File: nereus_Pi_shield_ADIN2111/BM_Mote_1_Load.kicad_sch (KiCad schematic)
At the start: 10 parts, among them U9 FPF2700MX

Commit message: S5.a: payload load switch U9 FPF2700MX (obsolete) -> U11 TPS26621DRCR; R11 DNP; Sofar brief
Load Switch sheet: U11 TI TPS26621DRCR (JLC C1848341) on new project
symbol nereus:TPS26621DRCR, stock Texas_DRC0010J footprint; R34 9.09k
(0.73 A); R41 1M IN->UVLO; dVdT NC; R32 pull-up -> R42 pull-down (SHDN
active low, payload off by default); SW_PGOOD/R33/TP34 removed. Top-Level:
R11 DNP, SW_PGOOD sheet pin removed. D18. ERC 74/626, netcheck 50/50,
kept parts identical. New docs/design-review/sofar_brief.md (mote vs
shield deviations for Sofar) + TRACKER rule.

Co-Authored-By: Claude Opus 5.5 <noreply@anthropic.com>
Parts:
- removed R33: RMCF0402FT100K, FP-RMCF0402-IPC_C, symbol BM_Mote_000639-AB-altium-import:Load_1_1029c3af85768c4190bb7ad29bc67b5_Altium C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
- removed TP34: TEST_POINT, PCB_TP_1.5mm, symbol BM_Mote_000639-AB-altium-import:Load_1_TEST_POINT_Sofar Ocean Technologies, Inc.
- removed U9: FPF2700MX, FAIR-SO-8_V, symbol BM_Mote_000639-AB-altium-import:Load_0_FAIR-FPF27XX-SOP-8_Altium Content Vault
- added R41: 1M, Resistor_SMD:R_0402_1005Metric, symbol Device:R
- added U11: TPS26621DRCR, Package_SON:Texas_DRC0010J, symbol nereus:TPS26621DRCR
- R34: value RC0402FR-07374KL -> RC0402FR-079K09L; RESISTANCE 374k -> 9.09kR
- renumbered R32 to R42
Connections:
- net GND: now also U11.11 (EP), U11.3 (OVP), U11.5 (RTN), U11.6 (GND)
- net ISET: now also U11.7 (ILIM)
- net SW_EN: now also U11.4 (~{SHDN})
- net SW_FLAGB: now also U11.9 (~{FLT})
- net VBUS_OUT: now also U11.10 (OUT)
- net VIN: now also R41.1, U11.1 (IN)
- new net: R41.2, U11.2 (UVLO)
- no-connect marks 0 -> 1

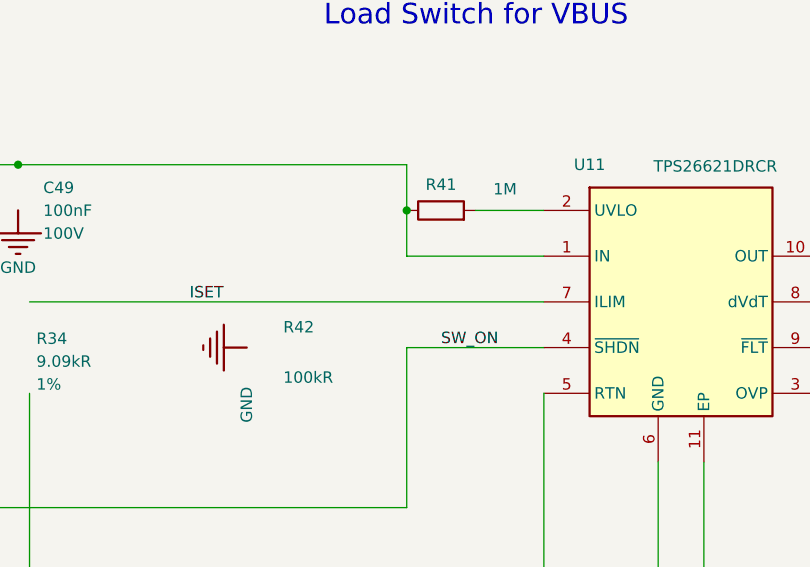
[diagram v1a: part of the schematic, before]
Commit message: S5.a: fix QE round 1 (R34 PART NUMBER, R42 10k worst-case SHDN, RTN=GND, N6, stale docs)
Co-Authored-By: Claude Opus 5.5 <noreply@anthropic.com>
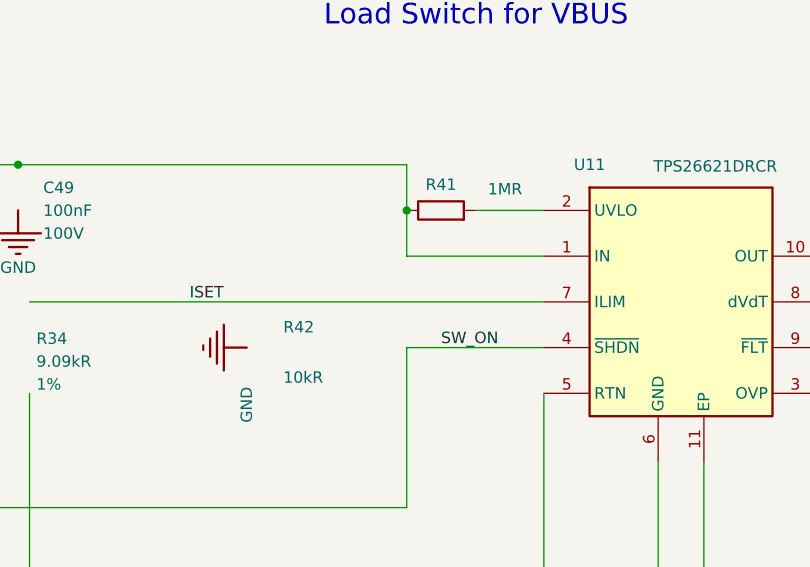
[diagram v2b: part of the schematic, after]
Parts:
- R34: PART NUMBER RC0402FR-07374KL -> RC0402FR-079K09L
- R41: value 1M -> RC0402FR-071ML; MPN RC0402FR-071ML -> (none); PART NUMBER (none) -> RC0402FR-071ML; RESISTANCE (none) -> 1MR
- R42: value RMCF0402FT100K -> RMCF0402FT10K0; RESISTANCE 100kR -> 10kR
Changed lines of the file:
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@@
 			)
 		)
-		(property "Value" "RMCF0402FT100K"
+		(property "Value" "RMCF0402FT10K0"
 			(at 177.292 153.2382 0)
 			(effects
@@
 			)
 		)
-		(property "Description" "RES 100K OHM 1% 0402: SW_ON pull-down, payload off by default (TPS26621 SHDN active low, D18)"
+		(property "Description" "RES 10K OHM 1% 0402: SW_ON pull-down, payload off by default. Worst case SHDN source 10 uA x 10k = 0.1 V < V(SHUTF) min 0.9 V (SLVSDT4F 7.5, D18)"
 			(at 195.58 154.7622 0)
 			(effects
@@
 			)
 		)
-		(property "RESISTANCE" "100kR"
+		(property "RESISTANCE" "10kR"
 			(at 181.864 158.8262 0)
 			(effects
@@
 			)
 		)
-		(property "PART NUMBER" "RC0402FR-07374KL"
+		(property "PART NUMBER" "RC0402FR-079K09L"
 			(at 152.908 149.1742 0)
 			(effects
@@
 			)
 		)
-		(property "Value" "1M"
+		(property "Value" "RC0402FR-071ML"
 			(at 206.502 137.16 90)
 			(effects
@@
 					(size 1.27 1.27)
 				)
+				(hide yes)
 			)
 		)
@@
 			)
 		)
-		(property "MPN" "RC0402FR-071ML"
-			(at 199.39 139.5222 0)
-			(effects
-				(font
-					(size 1.27 1.27)
-				)
-				(hide yes)
-			)
-		)
 		(property "MANUFACTURER" "Yageo"
 			(at 199.39 139.5222 0)
 			(effects
+				(font
+					(size 1.27 1.27)
+				)
+				(hide yes)
+			)
+		)
+		(property "RESISTANCE" "1MR"
+			(at 206.502 137.16 90)
+			(effects
+				(font
+					(size 1.27 1.27)
+				)
+			)
+		)
+		(property "PART NUMBER" "RC0402FR-071ML"
+			(at 199.39 139.5222 0)
+			(effects

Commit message: S4.d: footprints findable -- project library Vault (mote.pretty) extracted from the mote board; close S5.a
43 footprints the schematic uses, extracted read-only from the reference
board with KiCad 9.0.6 pcbnew (tools/fpextract.py, back-side parts
flipped, nets cleared), registered as nickname Vault to match the board
IDs; 118 bare footprint fields -> Vault:<name>. fpextract --verify: 0
problems (negative-tested). Netlist identical except footprint fields.
ERC 74/626 -> 74/508 (footprint-link warnings gone). D19.

Co-Authored-By: Claude Opus 5.5 <noreply@anthropic.com>
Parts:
- C49, C50: footprint FP-GRM188-0_1-e0_2_0_5-IPC_B -> Vault:FP-GRM188-0_1-e0_2_0_5-IPC_B
- D3: footprint FP-PMDTM-MFG -> Vault:FP-PMDTM-MFG
- R34: footprint RESC1005X40X25LL05T10 -> Vault:RESC1005X40X25LL05T10
- R35, R42: footprint FP-RMCF0402-IPC_C -> Vault:FP-RMCF0402-IPC_C
- TP35: footprint PCB_TP_1.5mm -> Vault:PCB_TP_1.5mm
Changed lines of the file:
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@@
 			)
 		)
-		(property "Footprint" ""
+				(property "Footprint" ""
 			(at 292.1 149.6822 0)
 			(effects
@@
 			)
 		)
-		(property "Footprint" "PCB_TP_1.5mm"
+		(property "Footprint" "Vault:PCB_TP_1.5mm"
 			(at 279.4 175.0822 0)
 			(effects
@@
 			)
 		)
-		(property "Footprint" ""
+				(property "Footprint" ""
 			(at 196.85 180.1622 0)
 			(effects
@@
 			)
 		)
-		(property "Footprint" "FP-RMCF0402-IPC_C"
+		(property "Footprint" "Vault:FP-RMCF0402-IPC_C"
 			(at 195.58 154.7622 0)
 			(effects
@@
 			)
 		)
-		(property "Footprint" "FP-RMCF0402-IPC_C"
+		(property "Footprint" "Vault:FP-RMCF0402-IPC_C"
 			(at 279.4 172.5422 0)
 			(effects
@@
 			)
 		)
-		(property "Footprint" ""
+				(property "Footprint" ""
 			(at 177.8 154.7622 0)
 			(effects
@@
 			)
 		)
-		(property "Footprint" ""
+				(property "Footprint" ""
 			(at 152.4 139.5222 0)
 			(effects
@@
 			)
 		)
-		(property "Footprint" "FP-PMDTM-MFG"
+		(property "Footprint" "Vault:FP-PMDTM-MFG"
 			(at 292.1 149.6822 0)
 			(effects
@@
 			)
 		)
-		(property "Footprint" ""
+				(property "Footprint" ""
 			(at 271.78 139.5222 0)
 			(effects
@@
 			)
 		)
-		(property "Footprint" "FP-GRM188-0_1-e0_2_0_5-IPC_B"
+		(property "Footprint" "Vault:FP-GRM188-0_1-e0_2_0_5-IPC_B"
 			(at 271.78 134.4422 0)
 			(effects
@@
 			)
 		)
-		(property "Footprint" "RESC1005X40X25LL05T10"
+		(property "Footprint" "Vault:RESC1005X40X25LL05T10"
 			(at 151.13 157.3022 0)
 			(effects
@@
 			)
 		)
-		(property "Footprint" ""
+				(property "Footprint" ""
 			(at 279.4 154.7622 0)
 			(effects
@@
 			)
 		)
-		(property "Footprint" "FP-GRM188-0_1-e0_2_0_5-IPC_B"
+		(property "Footprint" "Vault:FP-GRM188-0_1-e0_2_0_5-IPC_B"
 			(at 152.4 134.4422 0)
 			(effects
@@
 			)
 		)
-		(property "Footprint" "Package_SON:Texas_DRC0010J"
+				(property "Footprint" "Package_SON:Texas_DRC0010J"
 			(at 226.06 149.6822 0)
 			(effects
@@
 			)
 		)
-		(property "Footprint" "Resistor_SMD:R_0402_1005Metric"
+				(property "Footprint" "Resistor_SMD:R_0402_1005Metric"
 			(at 199.39 139.5222 0)
 			(effects

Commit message: S5.h: BOM alternates as hidden ALT/SOURCING fields; tracked bom.csv
- 24 flagged passives: hidden ALT1/ALT2 MPN/MFR/LCSC, ALT NOTE, SOURCING
  (values from docs/design-review/bom_alternates.md, D26)
- Critical parts (U1-U3, L3/L6, Y1, D1-D3, MP1-MP4, J5, J1): SOURCING only
- tools/check.sh exports docs/design-review/bom.csv: specified part first,
  alternates beside it; grouped by Value + DNP (R11 apart from R12/R13/R17/R19)
- J1 Footprint property re-indented (whitespace; import leftover)
- Fields only: ERC 531/27/504 unchanged, netcheck 51/51, midwire 0;
  netlist diff = the 208 new fields
- Docs: bom_alternates, bom_lifecycle, sofar_brief, changelog, DESIGN,
  TRACKER, viewer, DEV_LOG

Co-Authored-By: Claude Opus 5.5 <noreply@anthropic.com>
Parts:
- D3: SOURCING (none) -> JLC global sourcing (D26); no LCSC listing
- R34: ALT NOTE (none) -> 9.09 kΩ ±1 % 62.5 mW 50 V ±100 ppm thick film; our part (D1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; ALT1 LCSC (none) -> C227284; ALT1 MFR (none) -> YAGEO; ALT1 MPN (none) -> AC0402FR-079K09L; ALT2 LCSC (none) -> C11549; ALT2 MFR (none) -> UNI-ROYAL; ALT2 MPN (none) -> 0402WGF9091TCE; SOURCING (none) -> JLC global sourcing (first build) until an ALT is approved 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
- R35: ALT NOTE (none) -> 100 kΩ ±1 % 62.5 mW 50 V ±100 ppm; ALT1 is JLC Basic; AEC-Q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; ALT1 LCSC (none) -> C25741; ALT1 MFR (none) -> UNI-ROYAL; ALT1 MPN (none) -> 0402WGF1003TCE; ALT2 LCSC (none) -> C60491; ALT2 MFR (none) -> YAGEO; ALT2 MPN (none) -> RC0402FR-07100KL; SOURCING (none) -> JLC global sourcing (first build) until an ALT is approved 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
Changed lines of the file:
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@@
+			)
+		)
+		(property "ALT1 MPN" "0402WGF1003TCE"
+			(at 279.4 172.5422 0)
+			(effects
+				(font
+					(size 1.27 1.27)
+				)
+				(hide yes)
+			)
+		)
+		(property "ALT1 MFR" "UNI-ROYAL"
+			(at 279.4 172.5422 0)
+			(effects
+				(font
+					(size 1.27 1.27)
+				)
+				(hide yes)
+			)
+		)
+		(property "ALT1 LCSC" "C25741"
+			(at 279.4 172.5422 0)
+			(effects
+				(font
+					(size 1.27 1.27)
+				)
+				(hide yes)
+			)
+		)
+		(property "ALT2 MPN" "RC0402FR-07100KL"
+			(at 279.4 172.5422 0)
+			(effects
+				(font
+					(size 1.27 1.27)
+				)
+				(hide yes)
+			)
+		)
+		(property "ALT2 MFR" "YAGEO"
+			(at 279.4 172.5422 0)
+			(effects
+				(font
+					(size 1.27 1.27)
+				)
+				(hide yes)
+			)
+		)
+		(property "ALT2 LCSC" "C60491"
+			(at 279.4 172.5422 0)
+			(effects
+				(font
+					(size 1.27 1.27)
+				)
+				(hide yes)
+			)
+		)
+		(property "ALT NOTE" "100 kΩ ±1 % 62.5 mW 50 V ±100 ppm; ALT1 is JLC Basic; AEC-Q200 not stated (Stackpole is)"
+			(at 279.4 172.5422 0)
+			(effects
+				(font
+					(size 1.27 1.27)
+				)
+				(hide yes)
+			)
+		)
+		(property "SOURCING" "JLC global sourcing (first build) until an ALT is approved (D26)"
+			(at 279.4 172.5422 0)
+			(effects
+				(font
+					(size 1.27 1.27)
+				)
+				(hide yes)
 			)
 		)
@@
 			)
 		)
+		(property "SOURCING" "JLC global sourcing (D26); no LCSC listing"
+			(at 292.1 149.6822 0)
+			(effects
+				(font
+					(size 1.27 1.27)
+				)
+				(hide yes)
+			)
+		)
 		(pin "2"
 		)
@@
 				(hide yes)
 			)
+		)
+		(property "ALT1 MPN" "AC0402FR-079K09L"
+			(at 151.13 157.3022 0)
+			(effects
+				(font
+					(size 1.27 1.27)
+				)
+				(hide yes)
+			)
+		)
+		(property "ALT1 MFR" "YAGEO"
+			(at 151.13 157.3022 0)
+			(effects
+				(font
+					(size 1.27 1.27)
+				)
+				(hide yes)
+			)
+		)
+		(property "ALT1 LCSC" "C227284"
+			(at 151.13 157.3022 0)
+			(effects
+				(font
+					(size 1.27 1.27)
+				)
+				(hide yes)
+			)
+		)
+		(property "ALT2 MPN" "0402WGF9091TCE"
+			(at 151.13 157.3022 0)
+			(effects
+				(font
+					(size 1.27 1.27)
+				)
+				(hide yes)
+			)
+		)
+		(property "ALT2 MFR" "UNI-ROYAL"
+			(at 151.13 157.3022 0)
+			(effects
+				(font
+					(size 1.27 1.27)
+				)
+				(hide yes)
+			)
+		)
+		(property "ALT2 LCSC" "C11549"
+			(at 151.13 157.3022 0)
+			(effects
+				(font
+					(size 1.27 1.27)
+				)
+				(hide yes)
+			)
+		)
+		(property "ALT NOTE" "9.09 kΩ ±1 % 62.5 mW 50 V ±100 ppm thick film; our part (D18), no amendment"
+			(at 151.13 157.3022 0)
+			(effects
+				(font
+					(size 1.27 1.27)
+				)
+				(hide yes)
+			)
+		)
+		(property "SOURCING" "JLC global sourcing (first build) until an ALT is approved (D26)"
+			(at 151.13 157.3022 0)
+			(effects
+				(font
+					(size 1.27 1.27)
+				)
+				(hide yes)
+			)

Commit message: S5.i: planned part per BOM line (D27) beside Sofar's specified part
- PLANNED MPN/MFR/LCSC + PLANNED NOTE (why) on all 106 purchased parts;
  Value (Sofar's part) unchanged
- 10 lines planned as LCSC-stocked equivalents (R34, R20/R39, R21 group,
  C31, C17/C26, C21, C16 group, C19/C27, R14/R18) and D1 -> Sofar's Vishay
  second source; R8 kept (no ROHM land pattern); J1 TBD; rest as specified
- SOURCING on the 19 changed-line parts: planned part after Sofar approves
- Footprint lines of U11, R41, C56-C58 re-indented (whitespace only)
- View "Sofar review (planned parts)"; check.sh exports bom.csv from it
- Fields only: ERC 531/27/504 unchanged, netcheck 51/51, midwire 0
- Docs: DESIGN D27, bom_alternates, bom_lifecycle, sofar_brief, changelog,
  TRACKER, viewer, DEV_LOG

Co-Authored-By: Claude Opus 5.5 <noreply@anthropic.com>
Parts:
- C49, C50: PLANNED LCSC (none) -> C77058; PLANNED MFR (none) -> Murata; PLANNED MPN (none) -> GRM188R72A104KA35D; PLANNED NOTE (none) -> As specified; in LCSC stock (checked 2026-10-06)
- D3: PLANNED MFR (none) -> ROHM; PLANNED MPN (none) -> RB058LAM-60TFTR; PLANNED NOTE (none) -> As specified; JLC global sourcing (D26): no LCSC listing
- R34: PLANNED LCSC (none) -> C227284; PLANNED MFR (none) -> YAGEO; PLANNED MPN (none) -> AC0402FR-079K09L; PLANNED NOTE (none) -> Same YAGEO 0402 thick-film family, 9.09 kΩ ±1 % 62.5 mW 50 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; SOURCING JLC global sourcing (first build) until an ALT is approved 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 -> Planned part from LCSC once Sofar approves it (D27); until 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
- R35: PLANNED LCSC (none) -> C25741; PLANNED MFR (none) -> UNI-ROYAL; PLANNED MPN (none) -> 0402WGF1003TCE; PLANNED NOTE (none) -> JLC Basic part (no extended-part fee), largest LCSC stock; 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; SOURCING JLC global sourcing (first build) until an ALT is approved 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 -> Planned part from LCSC once Sofar approves it (D27); until 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
- R41: PLANNED LCSC (none) -> C138033; PLANNED MFR (none) -> Yageo; PLANNED MPN (none) -> RC0402FR-071ML; PLANNED NOTE (none) -> As specified; in LCSC stock (checked 2026-10-06)
- R42: PLANNED LCSC (none) -> C6111655; PLANNED MFR (none) -> Stackpole; PLANNED MPN (none) -> RMCF0402FT10K0; PLANNED NOTE (none) -> As specified; in LCSC stock (checked 2026-10-06)
- U11: PLANNED LCSC (none) -> C1848341; PLANNED MFR (none) -> Texas Instruments; PLANNED MPN (none) -> TPS26621DRCR; PLANNED NOTE (none) -> As specified; in LCSC stock (checked 2026-10-06)

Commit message: S5.i: QE round 1 APPROVED WITH NITS -- notes fixed; record report; S5 complete
- F1: R21 group "ample LCSC stock"; C16 group stock figures stated
- N1: C17/C26 note no longer claims the same part (thickness not confirmed)
- N2: D26 marked "amended by D27"; N3: C21 note reworded
- R8 datasheet URLs in bom_alternates.md
- QE report in docs/design-review/qe/S5.md; TRACKER, viewer, DEV_LOG

Co-Authored-By: Claude Opus 5.5 <noreply@anthropic.com>
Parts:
- R35: PLANNED NOTE JLC Basic part (no extended-part fee), largest LCSC stock; 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 -> JLC Basic part (no extended-part fee), ample LCSC stock; 10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
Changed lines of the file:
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@@
 			)
 		)
-		(property "PLANNED NOTE" "JLC Basic part (no extended-part fee), largest LCSC stock; 100 kΩ ±1 % 62.5 mW 50 V ±100 ppm 0402; specified Stackpole is out of stock at LCSC and is AEC-Q200, this one doesn't state it"
+		(property "PLANNED NOTE" "JLC Basic part (no extended-part fee), ample LCSC stock; 100 kΩ ±1 % 62.5 mW 50 V ±100 ppm 0402; specified Stackpole is out of stock at LCSC and is AEC-Q200, this one doesn't state it"
 			(at 279.4 172.5422 0)
 			(effects

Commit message: S6.a: BOM hygiene -- TP/FID/MTG out of the BOM; MANUFACTURER filled
- in_bom no on TP x16, FID1-6, MTG1-4 (bare copper / holes)
- MANUFACTURER on the 75 BOM parts without one, from bom_lifecycle.md;
  Sofar's MFR_NAME / MANUFACTURER1 / MANUFACTURER 1 untouched; J1 open
- bom.csv 51 rows, Mfr on every row but J1
- ERC 531/27/504 unchanged, netcheck 51/51, midwire 0
- Docs: bom_lifecycle, changelog, DESIGN, TRACKER (S6 bites), viewer, DEV_LOG

Co-Authored-By: Claude Opus 5.5 <noreply@anthropic.com>
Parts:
- C49, C50: MANUFACTURER (none) -> Murata
- D3: MANUFACTURER (none) -> ROHM
- R35, R42: MANUFACTURER (none) -> Stackpole
- TP35: now left out of the parts list
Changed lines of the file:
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@@
 		(unit 0)
 		(exclude_from_sim no)
-		(in_bom yes)
+		(in_bom no)
 		(on_board yes)
 		(dnp no)
@@
 			)
 		)
+		(property "MANUFACTURER" "Stackpole"
+			(at 195.58 154.7622 0)
+			(effects
+				(font
+					(size 1.27 1.27)
+				)
+				(hide yes)
+			)
+		)
 		(pin "1"
 		)
@@
 			)
 		)
+		(property "MANUFACTURER" "Stackpole"
+			(at 279.4 172.5422 0)
+			(effects
+				(font
+					(size 1.27 1.27)
+				)
+				(hide yes)
+			)
+		)
 		(pin "1"
 		)
@@
 			)
 		)
+		(property "MANUFACTURER" "ROHM"
+			(at 292.1 149.6822 0)
+			(effects
+				(font
+					(size 1.27 1.27)
+				)
+				(hide yes)
+			)
+		)
 		(pin "2"
 		)
@@
 			)
 		)
+		(property "MANUFACTURER" "Murata"
+			(at 271.78 134.4422 0)
+			(effects
+				(font
+					(size 1.27 1.27)
+				)
+				(hide yes)
+			)
+		)
 		(pin "1"
 		)
@@
 			(at 152.4 134.4422 0)
 			(effects
+				(font
+					(size 1.27 1.27)
+				)
+				(hide yes)
+			)
+		)
+		(property "MANUFACTURER" "Murata"
+			(at 152.4 134.4422 0)
+			(effects
